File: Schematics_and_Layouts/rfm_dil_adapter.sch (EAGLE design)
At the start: 17 parts

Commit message: Added Gerber Files
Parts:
- renumbered CLK to IO5, DCLK to IO1, FSK to IO2, GND1 to AGND, NINT to IO3, NIRQ to IO0, NRES to RES, NSEL to NSS, SDI to MOSI, SDO to MISO
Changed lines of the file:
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@@
 <?xml version="1.0" encoding="utf-8"?>
 <!DOCTYPE eagle SYSTEM "eagle.dtd">
-<eagle version="6.3">
+<eagle version="6.6.0">
 <drawing>
 <settings>
@@
 <parts>
 <part name="U$1" library="fp" deviceset="RFM12_Z" device=""/>
-<part name="CLK" library="solpad" deviceset="SE13" device=""/>
-<part name="DCLK" library="solpad" deviceset="SE13" device=""/>
-<part name="FSK" library="solpad" deviceset="SE13" device=""/>
-<part name="SDI" library="solpad" deviceset="SE13" device=""/>
-<part name="SDO" library="solpad" deviceset="SE13" device=""/>
+<part name="IO5" library="solpad" deviceset="SE13" device=""/>
+<part name="IO1" library="solpad" deviceset="SE13" device=""/>
+<part name="IO2" library="solpad" deviceset="SE13" device=""/>
+<part name="MOSI" library="solpad" deviceset="SE13" device=""/>
+<part name="MISO" library="solpad" deviceset="SE13" device=""/>
 <part name="SCK" library="solpad" deviceset="SE13" device=""/>
-<part name="NSEL" library="solpad" deviceset="SE13" device=""/>
+<part name="NSS" library="solpad" deviceset="SE13" device=""/>
 <part name="GND" library="solpad" deviceset="SE13" device=""/>
-<part name="GND1" library="solpad" deviceset="SE13" device=""/>
-<part name="NRES" library="solpad" deviceset="SE13" device=""/>
-<part name="NIRQ" library="solpad" deviceset="SE13" device=""/>
-<part name="NINT" library="solpad" deviceset="SE13" device=""/>
+<part name="AGND" library="solpad" deviceset="SE13" device=""/>
+<part name="RES" library="solpad" deviceset="SE13" device=""/>
+<part name="IO0" library="solpad" deviceset="SE13" device=""/>
+<part name="IO3" library="solpad" deviceset="SE13" device=""/>
 <part name="VDD" library="solpad" deviceset="SE13" device=""/>
 <part name="ANT+" library="testpad" deviceset="PTR1" device="TP20SQ"/>
@@
 <instances>
 <instance part="U$1" gate="G$1" x="71.12" y="48.26"/>
-<instance part="CLK" gate="1" x="48.26" y="43.18" rot="R90"/>
-<instance part="DCLK" gate="1" x="48.26" y="48.26" rot="R90"/>
-<instance part="FSK" gate="1" x="48.26" y="50.8" rot="R90"/>
-<instance part="SDI" gate="1" x="48.26" y="55.88" rot="R90"/>
-<instance part="SDO" gate="1" x="48.26" y="58.42" rot="R90"/>
+<instance part="IO5" gate="1" x="48.26" y="43.18" rot="R90"/>
+<instance part="IO1" gate="1" x="48.26" y="48.26" rot="R90"/>
+<instance part="IO2" gate="1" x="48.26" y="50.8" rot="R90"/>
+<instance part="MOSI" gate="1" x="48.26" y="55.88" rot="R90"/>
+<instance part="MISO" gate="1" x="48.26" y="58.42" rot="R90"/>
 <instance part="SCK" gate="1" x="48.26" y="60.96" rot="R90"/>
-<instance part="NSEL" gate="1" x="48.26" y="66.04" rot="R90"/>
+<instance part="NSS" gate="1" x="48.26" y="66.04" rot="R90"/>
 <instance part="GND" gate="1" x="66.04" y="27.94" rot="R90"/>
-<instance part="GND1" gate="1" x="76.2" y="27.94" rot="R270"/>
-<instance part="NRES" gate="1" x="96.52" y="58.42" rot="R270"/>
-<instance part="NIRQ" gate="1" x="96.52" y="63.5" rot="R270"/>
-<instance part="NINT" gate="1" x="96.52" y="66.04" rot="R270"/>
+<instance part="AGND" gate="1" x="76.2" y="27.94" rot="R270"/>
+<instance part="RES" gate="1" x="96.52" y="58.42" rot="R270"/>
+<instance part="IO0" gate="1" x="96.52" y="63.5" rot="R270"/>
+<instance part="IO3" gate="1" x="96.52" y="66.04" rot="R270"/>
 <instance part="VDD" gate="1" x="71.12" y="76.2"/>
 <instance part="ANT+" gate="G$1" x="93.98" y="40.64"/>
@@
 <segment>
 <pinref part="U$1" gate="G$1" pin="CLK"/>
-<pinref part="CLK" gate="1" pin="MP"/>
+<pinref part="IO5" gate="1" pin="MP"/>
 </segment>
 </net>
@@
 <segment>
 <pinref part="U$1" gate="G$1" pin="DCLK/CFIL/FFIT"/>
-<pinref part="DCLK" gate="1" pin="MP"/>
+<pinref part="IO1" gate="1" pin="MP"/>
 </segment>
 </net>
@@
 <segment>
 <pinref part="U$1" gate="G$1" pin="FSK/DATA/NFFS"/>
-<pinref part="FSK" gate="1" pin="MP"/>
+<pinref part="IO2" gate="1" pin="MP"/>
 </segment>
 </net>
@@
 <segment>
 <pinref part="U$1" gate="G$1" pin="SDI"/>
-<pinref part="SDI" gate="1" pin="MP"/>
+<pinref part="MOSI" gate="1" pin="MP"/>
 </segment>
 </net>
@@
 <segment>
 <pinref part="U$1" gate="G$1" pin="SDO"/>
-<pinref part="SDO" gate="1" pin="MP"/>
+<pinref part="MISO" gate="1" pin="MP"/>
 </segment>
 </net>
@@
 <segment>
 <pinref part="U$1" gate="G$1" pin="NSEL/"/>
-<pinref part="NSEL" gate="1" pin="MP"/>
+<pinref part="NSS" gate="1" pin="MP"/>
 </segment>
 </net>
@@
 <segment>
 <pinref part="U$1" gate="G$1" pin="NRES"/>
-<pinref part="NRES" gate="1" pin="MP"/>
+<pinref part="RES" gate="1" pin="MP"/>
 </segment>
 </net>
@@
 <segment>
 <pinref part="U$1" gate="G$1" pin="NIRQ"/>
-<pinref part="NIRQ" gate="1" pin="MP"/>
+<pinref part="IO0" gate="1" pin="MP"/>
 </segment>
 </net>
@@
 <segment>
 <pinref part="U$1" gate="G$1" pin="NINT"/>
-<pinref part="NINT" gate="1" pin="MP"/>
+<pinref part="IO3" gate="1" pin="MP"/>
 </segment>
 </net>
@@
 <segment>
 <pinref part="U$1" gate="G$1" pin="GND1"/>
-<pinref part="GND1" gate="1" pin="MP"/>
+<pinref part="AGND" gate="1" pin="MP"/>
 <pinref part="GND3" gate="1" pin="GND"/>
 <wire x1="73.66" y1="25.4" x2="73.66" y2="27.94" width="0.1524" layer="91"/>

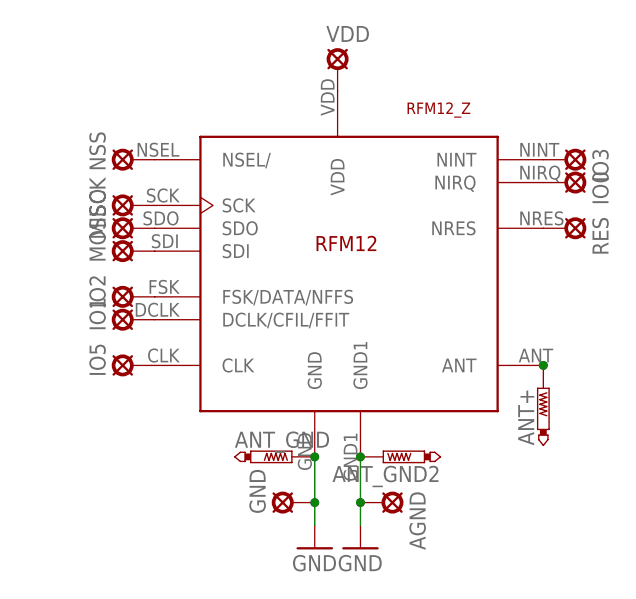
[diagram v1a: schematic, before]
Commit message: Angleichung von Handbuch und Layouts
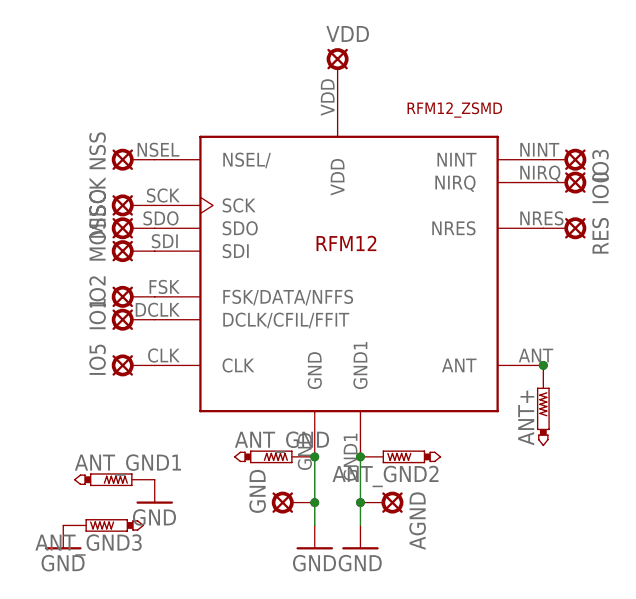
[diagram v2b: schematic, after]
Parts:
- added ANT_GND1, ANT_GND3: PTR1TP20SQ, testpad:PTR1TP20SQ
- AGND, GND, IO0, IO1, IO2, IO3, IO5, MISO, MOSI, NSS, RES, SCK, VDD: value SE13 -> LSP10; device solpad:SE13 -> solpad:LSP10
- U$1: value RFM12_Z -> RFM12_ZSMD; device fp:RFM12_Z -> fp:RFM12_ZSMD
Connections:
- net GND: now also ANT_GND1.TP, ANT_GND3.TP
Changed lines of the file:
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@@
 <layer number="97" name="Info" color="7" fill="1" visible="yes" active="yes"/>
 <layer number="98" name="Guide" color="6" fill="1" visible="yes" active="yes"/>
+<layer number="116" name="centerDrill" color="7" fill="1" visible="no" active="yes"/>
 </layers>
 <schematic xreflabel="%F%N/%S.%C%R" xrefpart="/%S.%C%R">
@@
 </classes>
 <parts>
-<part name="U$1" library="fp" deviceset="RFM12_Z" device=""/>
-<part name="IO5" library="solpad" deviceset="SE13" device=""/>
-<part name="IO1" library="solpad" deviceset="SE13" device=""/>
-<part name="IO2" library="solpad" deviceset="SE13" device=""/>
-<part name="MOSI" library="solpad" deviceset="SE13" device=""/>
-<part name="MISO" library="solpad" deviceset="SE13" device=""/>
-<part name="SCK" library="solpad" deviceset="SE13" device=""/>
-<part name="NSS" library="solpad" deviceset="SE13" device=""/>
-<part name="GND" library="solpad" deviceset="SE13" device=""/>
-<part name="AGND" library="solpad" deviceset="SE13" device=""/>
-<part name="RES" library="solpad" deviceset="SE13" device=""/>
-<part name="IO0" library="solpad" deviceset="SE13" device=""/>
-<part name="IO3" library="solpad" deviceset="SE13" device=""/>
-<part name="VDD" library="solpad" deviceset="SE13" device=""/>
+<part name="U$1" library="fp" deviceset="RFM12_Z" device="SMD"/>
+<part name="IO5" library="solpad" deviceset="LSP10" device=""/>
+<part name="IO1" library="solpad" deviceset="LSP10" device=""/>
+<part name="IO2" library="solpad" deviceset="LSP10" device=""/>
+<part name="MOSI" library="solpad" deviceset="LSP10" device=""/>
+<part name="MISO" library="solpad" deviceset="LSP10" device=""/>
+<part name="SCK" library="solpad" deviceset="LSP10" device=""/>
+<part name="NSS" library="solpad" deviceset="LSP10" device=""/>
+<part name="GND" library="solpad" deviceset="LSP10" device=""/>
+<part name="AGND" library="solpad" deviceset="LSP10" device=""/>
+<part name="RES" library="solpad" deviceset="LSP10" device=""/>
+<part name="IO0" library="solpad" deviceset="LSP10" device=""/>
+<part name="IO3" library="solpad" deviceset="LSP10" device=""/>
+<part name="VDD" library="solpad" deviceset="LSP10" device=""/>
 <part name="ANT+" library="testpad" deviceset="PTR1" device="TP20SQ"/>
 <part name="ANT_GND" library="testpad" deviceset="PTR1" device="TP20SQ"/>
@@
 <attribute name="TP_SIGNAL_NAME" value=""/>
 </part>
+<part name="ANT_GND1" library="testpad" deviceset="PTR1" device="TP20SQ"/>
+<part name="ANT_GND3" library="testpad" deviceset="PTR1" device="TP20SQ"/>
+<part name="GND1" library="supply1" deviceset="GND" device=""/>
+<part name="GND4" library="supply1" deviceset="GND" device=""/>
 </parts>
 <sheets>
@@
 <instance part="GND3" gate="1" x="73.66" y="22.86"/>
 <instance part="ANT_GND2" gate="G$1" x="76.2" y="33.02" rot="R90"/>
+<instance part="ANT_GND1" gate="G$1" x="48.26" y="30.48" rot="R270"/>
+<instance part="ANT_GND3" gate="G$1" x="43.18" y="25.4" rot="R90"/>
+<instance part="GND1" gate="1" x="40.64" y="22.86"/>
+<instance part="GND4" gate="1" x="50.8" y="27.94"/>
 </instances>
 <busses>
@@
 <pinref part="ANT_GND2" gate="G$1" pin="TP"/>
 </segment>
+<segment>
+<pinref part="ANT_GND3" gate="G$1" pin="TP"/>
+<pinref part="GND1" gate="1" pin="GND"/>
+</segment>
+<segment>
+<pinref part="ANT_GND1" gate="G$1" pin="TP"/>
+<pinref part="GND4" gate="1" pin="GND"/>
+</segment>
 </net>
